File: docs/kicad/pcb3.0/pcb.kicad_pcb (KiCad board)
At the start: 2 copper layers, 49.5 x 86.4 mm, 11 parts, among them J1 power, J2 coil1, J3 coil2, J4 halls1, J6 led, SW1 SW, U1 L293D, U2 ESP32_DEV

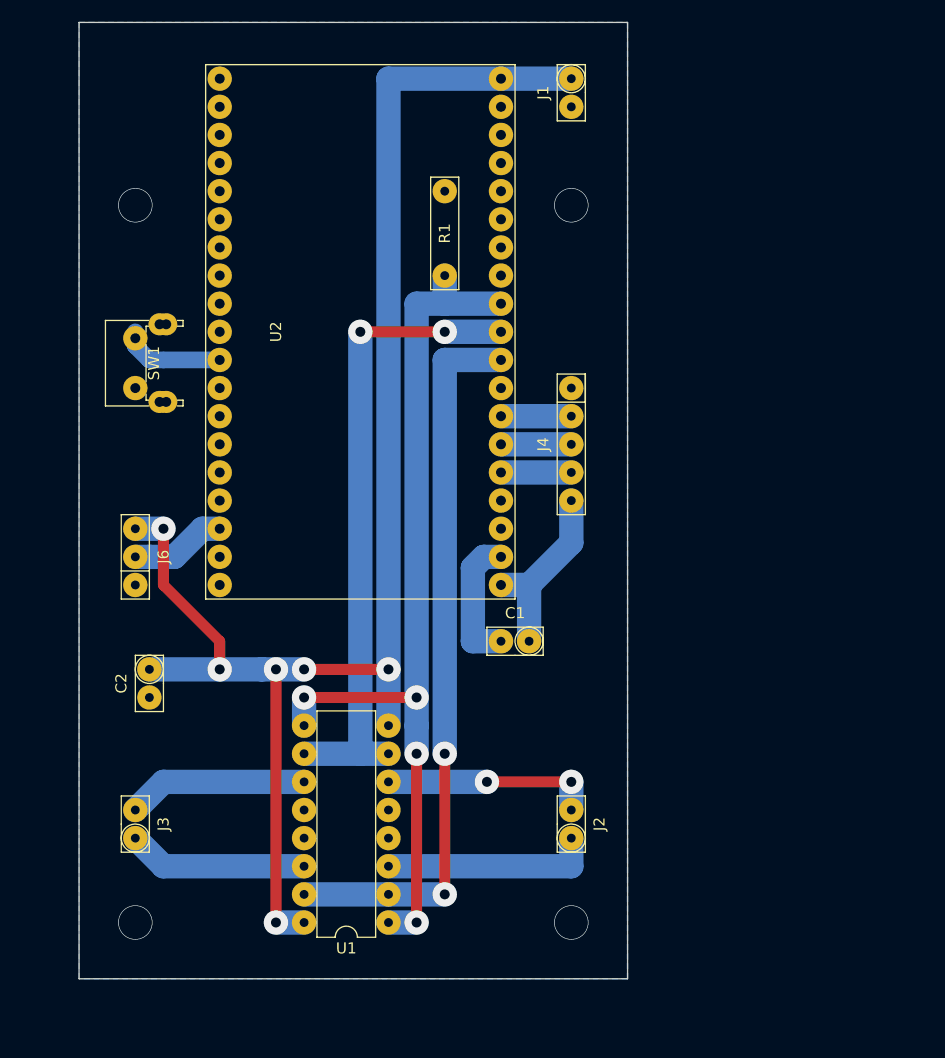
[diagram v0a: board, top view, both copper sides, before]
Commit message: initial v3 circuit board, pin assigments in code TODO: code in general
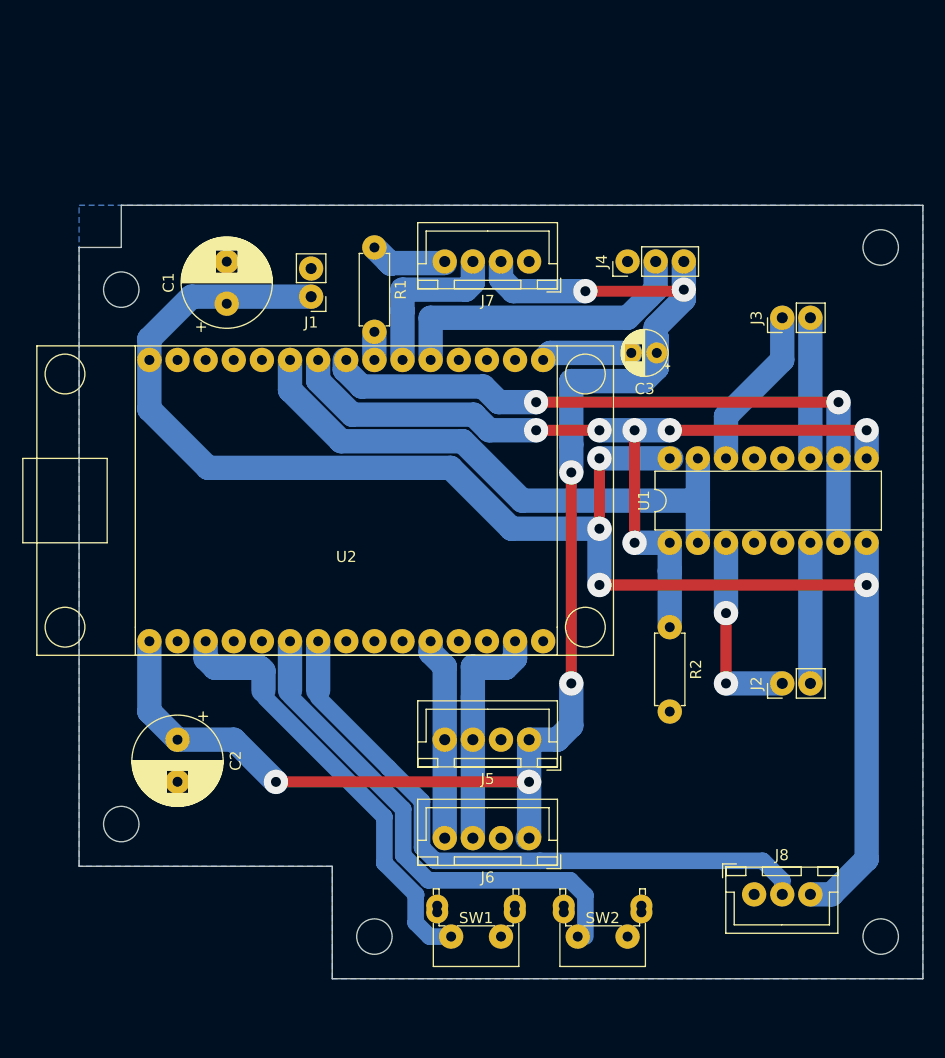
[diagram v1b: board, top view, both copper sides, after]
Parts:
- added C3: 10uf, 0_my_footprints:CP_my10uf, F.Cu at (52.1, -56.5)
- added J5: Sens1, 0_my_footprints:myJSTx04, F.Cu at (40.6, -21.6)
- added J7: Opto, 0_my_footprints:myJSTx04, F.Cu at (40.6, -64.8)
- added J8: leds, 0_my_footprints:myJSTx03, F.Cu at (61.0, -7.62)
- added R2: 10K, 0_my_footprints:myResistor, F.Cu at (53.3, -31.8)
- added REF**: myMountingHole_3.2mm_M3, 0_my_footprints:myMountingHole_3.2mm_M3, F.Cu at (3.81, -14.0)
- added REF**: myMountingHole_3.2mm_M3, 0_my_footprints:myMountingHole_3.2mm_M3, F.Cu at (3.81, -62.2)
- added REF**: myMountingHole_3.2mm_M3, 0_my_footprints:myMountingHole_3.2mm_M3, F.Cu at (26.7, -3.81)
- added REF**: myMountingHole_3.2mm_M3, 0_my_footprints:myMountingHole_3.2mm_M3, F.Cu at (72.4, -3.81)
- added REF**: myMountingHole_3.2mm_M3, 0_my_footprints:myMountingHole_3.2mm_M3, F.Cu at (72.4, -66.0)
- added SW2: SW, cnc3018-PCB:right_angle_button, F.Cu at (49.5, -3.81)
- C1: value 10uf -> 100uf; footprint cnc3018-PCB:my2pin -> 0_my_footprints:CP_my100uf
- C2: footprint cnc3018-PCB:my2pin -> 0_my_footprints:CP_my100uf
- J1, J2, J3: footprint cnc3018-PCB:my2pin -> 0_my_footprints:myPinHeader_1x02
- J4: value halls1 -> hall; footprint cnc3018-PCB:my5Pin -> 0_my_footprints:myPinHeader_1x03
- J6: value led -> Sens2; footprint cnc3018-PCB:my3pin -> 0_my_footprints:myJSTx04
- R1: value 10K -> 220; footprint cnc3018-PCB:myResistor -> 0_my_footprints:myResistor
- U1: footprint cnc3018-PCB:myDip16 -> 0_my_footprints:myDip16
- U2: value ESP32_DEV -> ESP32_DEV_0; footprint cnc3018-PCB:ESP32-DEV -> 0_my_footprints:myESP32DEV0
- moved J3 75.0 mm to (63.5, -59.7)
- moved SW1 59.5 mm to (38.1, -3.81), turned to 180 degrees
- moved J6 43.7 mm to (40.6, -12.7), turned to 180 degrees
- moved U1 42.7 mm to (53.3, -39.4), turned to 90 degrees
- moved C1 40.9 mm to (13.3, -61.0), turned to 90 degrees
- moved J1 30.7 mm to (21.0, -61.6), turned to 180 degrees
- moved J2 23.6 mm to (63.5, -26.7)
- moved J4 17.3 mm to (49.5, -64.8), turned to 90 degrees
- moved U2 15.3 mm to (24.1, -43.2), turned to 0 degrees
- moved R1 6.84 mm to (26.7, -66.0), turned to 270 degrees
- moved C2 6.84 mm to (8.89, -21.6)
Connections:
- net SW renamed SW1
- C1 pad 1: +3V3 -> +5V
- C1 pad 2: Net-(C1-Pad2) -> GND
- C2 pad 1: +5V -> +3V3
- J4 pad 2: hall1 -> hall
- J4 pad 3: hall2 -> +3V3
- J6 pad 1: GND -> +3V3
- J6 pad 2: LED -> GND
- J6 pad 3: +5V -> SCL
- R1 pad 1: EN -> Net-(J7-Pad4)
- R1 pad 2: GND -> SDIO
- U2 pad 10: I2 -> SCK
- U2 pad 11: I1 -> hall
- U2 pad 13: hall1 -> Net-(U2-Pad13)
- U2 pad 14: hall2 -> Net-(U2-Pad14)
- U2 pad 15: hall3 -> Net-(C3-Pad2)
- U2 pad 17: Net-(U2-Pad17) -> SCL
- U2 pad 18: Net-(C1-Pad2) -> Net-(U2-Pad18)
- U2 pad 19: +3V3 -> Net-(U2-Pad19)
- U2 pad 2: Net-(U2-Pad2) -> GND
- U2 pad 20: GND -> SDA
- U2 pad 22: LED -> Net-(U2-Pad22)
- U2 pad 24: Net-(U2-Pad24) -> LEDS
- U2 pad 25: Net-(U2-Pad25) -> SW2
- U2 pad 26: GND -> Net-(U2-Pad26)
- U2 pad 29: Net-(U2-Pad29) -> GND
- U2 pad 30: Net-(U2-Pad30) -> +3V3
- U2 pad 6: GND -> I1
- U2 pad 7: Net-(U2-Pad7) -> EN
- U2 pad 8: Net-(U2-Pad8) -> I2
- U2 pad 9: EN -> SDIO
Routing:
- net +3V3: track 16.8 -> 125.2 mm, vias 0 -> 6
- net LEDS: track 0.00 -> 56.9 mm
- net SW2: track 0.00 -> 44.7 mm
- net SW1: track 9.42 -> 38.7 mm
- net hall: track 0.00 -> 27.7 mm
- net SCL: track 0.00 -> 21.3 mm
- net SDA: track 0.00 -> 18.3 mm
- net SCK: track 0.00 -> 14.9 mm
- net I1: track 66.0 -> 51.3 mm, vias 2 -> 0
- net Net-(C1-Pad2): track 12.1 -> 0.00 mm
- net LED: track 8.67 -> 0.00 mm
- net Net-(C3-Pad2): track 0.00 -> 8.12 mm
- net Net-(J7-Pad4): track 0.00 -> 6.99 mm
- net OA2: track 19.1 -> 12.7 mm, vias 2 -> 0
- net hall3: track 6.35 -> 0.00 mm
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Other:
- board size 49.5 x 86.4 mm -> 76.2 x 69.8 mm

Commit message: create and build circuit board
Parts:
- removed the REF** at (3.81, -14.0)
- removed the REF** at (3.81, -62.2)
- removed the REF** at (26.7, -3.81)
- removed the REF** at (72.4, -3.81)
- added REF**: myMountingHole_3.2mm_M3, 0_my_footprints:myMountingHole_3.2mm_M3, F.Cu at (55.9, -3.81)
- added REF**: myMountingHole_3.2mm_M3, 0_my_footprints:myMountingHole_3.2mm_M3, F.Cu at (7.62, -3.81)
- added REF**: myMountingHole_3.2mm_M3, 0_my_footprints:myMountingHole_3.2mm_M3, F.Cu at (66.0, -26.7)
- added REF**: myMountingHole_3.2mm_M3, 0_my_footprints:myMountingHole_3.2mm_M3, F.Cu at (66.0, -72.4)
- moved REF** 68.9 mm to (3.81, -72.4), turned to 90 degrees
- moved J3 53.5 mm to (10.2, -63.5), turned to 180 degrees
- moved J8 53.4 mm to (62.2, -61.0), turned to 90 degrees
- moved SW2 48.6 mm to (66.0, -49.5), turned to 270 degrees
- moved C1 47.8 mm to (8.89, -13.3), turned to 180 degrees
- moved J4 47.0 mm to (5.08, -49.5), turned to 180 degrees
- moved R1 45.5 mm to (3.81, -26.7), turned to 0 degrees
- moved SW1 44.2 mm to (66.0, -38.1), turned to 270 degrees
- moved J7 43.0 mm to (5.08, -40.6), turned to 270 degrees
- moved J1 42.6 mm to (8.26, -21.0), turned to 270 degrees
- moved J2 42.1 mm to (43.2, -63.5), turned to 180 degrees
- moved C2 41.4 mm to (48.3, -8.89), turned to 0 degrees
- moved C3 39.0 mm to (13.3, -52.1), turned to 270 degrees
- moved J6 32.5 mm to (57.1, -40.6), turned to 270 degrees
- moved U1 26.8 mm to (30.5, -53.3), turned to 180 degrees
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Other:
- board size 76.2 x 69.8 mm -> 69.8 x 76.2 mm

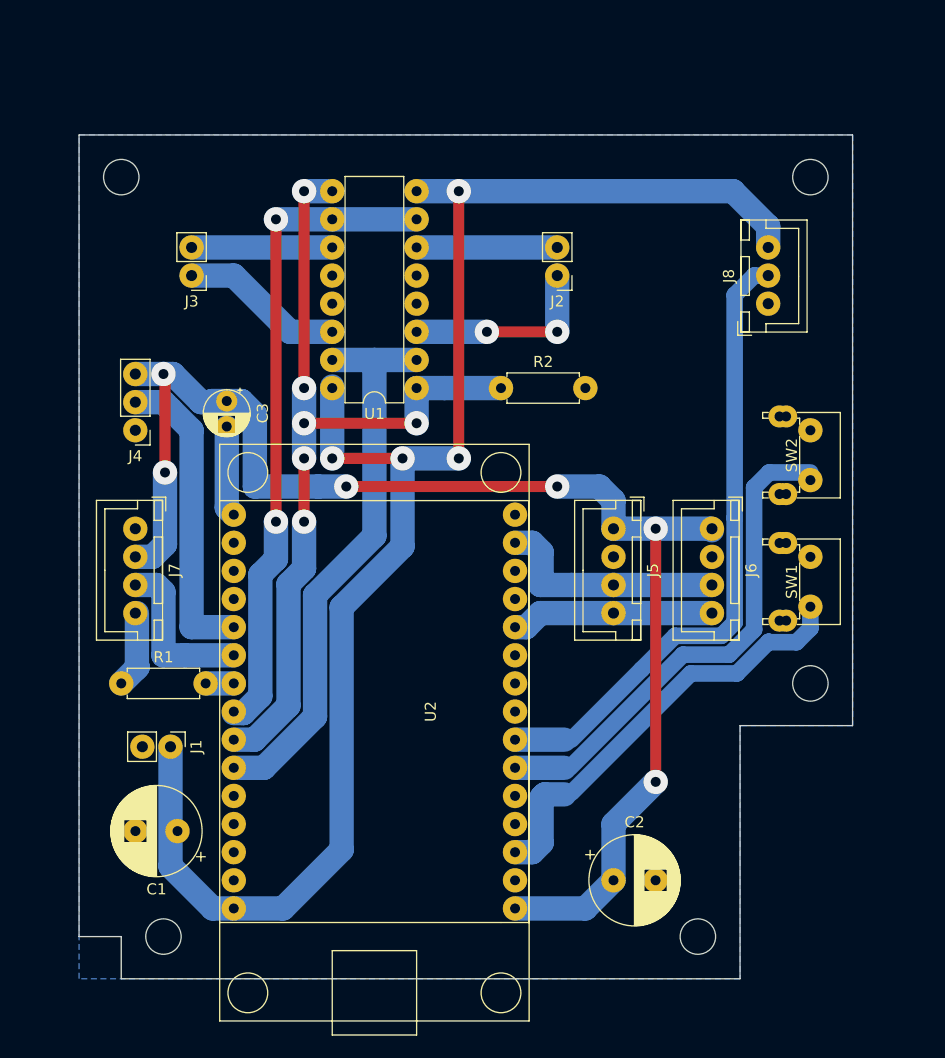
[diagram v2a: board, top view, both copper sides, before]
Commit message: change 3.1 to 3.0 and generate flatcam stuff
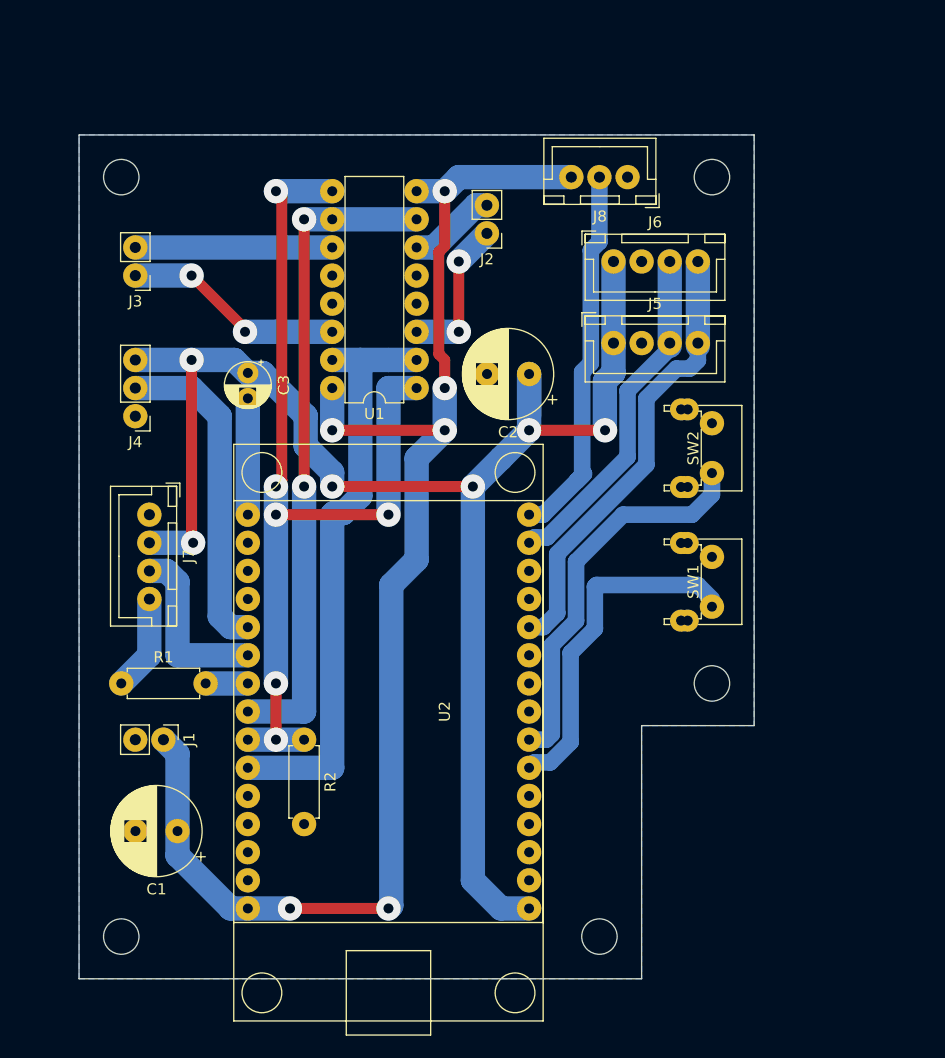
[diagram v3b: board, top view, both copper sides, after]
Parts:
- removed the REF** at (55.9, -3.81)
- removed the REF** at (7.62, -3.81)
- removed the REF** at (66.0, -26.7)
- removed the REF** at (66.0, -72.4)
- added REF**: myMountingHole_3.2mm_M3, 0_my_footprints:myMountingHole_3.2mm_M3, F.Cu at (47.0, -3.81)
- added REF**: myMountingHole_3.2mm_M3, 0_my_footprints:myMountingHole_3.2mm_M3, F.Cu at (3.81, -3.81)
- added REF**: myMountingHole_3.2mm_M3, 0_my_footprints:myMountingHole_3.2mm_M3, F.Cu at (57.1, -26.7)
- added REF**: myMountingHole_3.2mm_M3, 0_my_footprints:myMountingHole_3.2mm_M3, F.Cu at (57.1, -72.4)
- moved C2 46.4 mm to (40.6, -54.6), turned to 180 degrees
- moved R2 36.4 mm to (20.3, -21.6), turned to 270 degrees
- moved J6 25.7 mm to (48.3, -64.8), turned to 0 degrees
- moved J8 17.1 mm to (49.5, -72.4), turned to 180 degrees
- moved J5 16.8 mm to (48.3, -57.4), turned to 0 degrees
- moved SW2 8.91 mm to (57.1, -50.2)
- moved SW1 8.89 mm to (57.1, -38.1)
- moved J2 7.41 mm to (36.8, -67.3)
- moved J3 5.08 mm to (5.08, -63.5)
- moved C3 3.17 mm to (15.2, -54.6)
- moved J7 1.80 mm to (6.35, -41.9)
- moved U2 1.27 mm to (27.9, -24.1)
- moved J4 1.27 mm to (5.08, -50.8)
- moved J1 0.90 mm to (7.62, -21.6)
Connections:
- U2 pad 16: Net-(U2-Pad16) -> LEDS
- U2 pad 24: LEDS -> SW2
- U2 pad 25: SW2 -> SW1
- U2 pad 28: SW1 -> Net-(U2-Pad28)
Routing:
- net SDA: track 18.3 -> 41.0 mm
- net LEDS: track 56.9 -> 34.5 mm
- net +5V: track 144.7 -> 127.8 mm, vias 4 -> 6
- net +3V3: track 125.2 -> 138.5 mm
- net SCL: track 21.3 -> 31.3 mm
- net SW2: track 44.7 -> 35.5 mm
- net SW1: track 38.7 -> 30.8 mm
- net EN: track 76.7 -> 84.3 mm
- net OB1: track 14.8 -> 20.0 mm, vias 0 -> 2
- net OB2: track 12.7 -> 17.8 mm
- net OA2: track 12.7 -> 7.93 mm
- net OA1: track 17.8 -> 13.8 mm
- net I1: track 51.3 -> 53.6 mm
- net Net-(C3-Pad2): track 8.12 -> 10.2 mm
- net hall: track 27.7 -> 29.7 mm
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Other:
- board size 69.8 x 76.2 mm -> 61 x 76.2 mm
